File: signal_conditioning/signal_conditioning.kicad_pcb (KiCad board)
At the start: 2 copper layers, 16 parts, among them P1 CONN_6, P2 CONN_6, U1 LM324

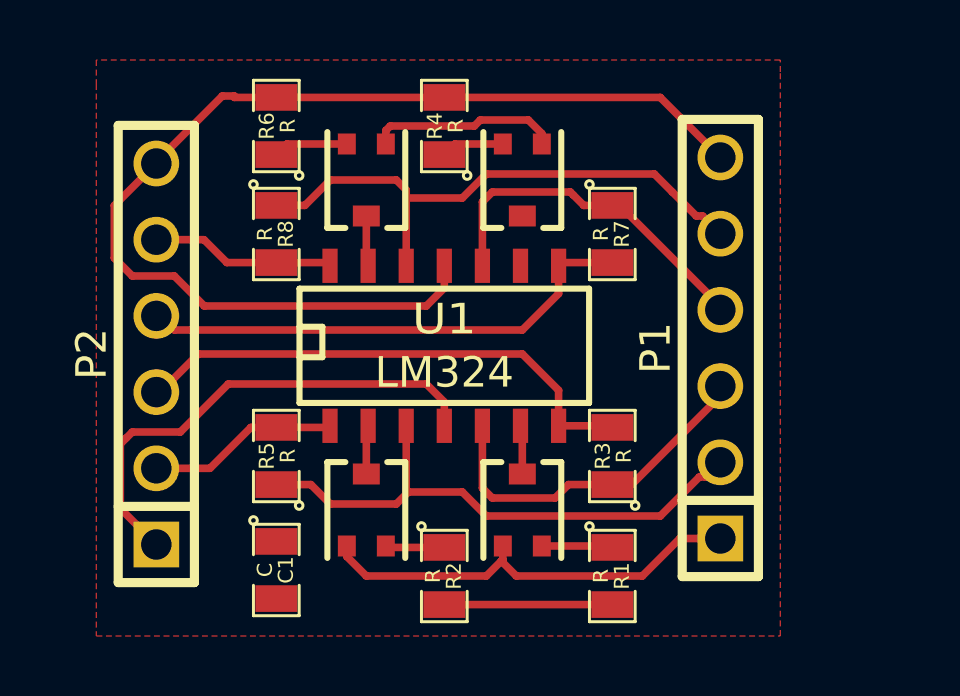
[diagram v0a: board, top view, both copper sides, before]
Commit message: rc version with pull ups input
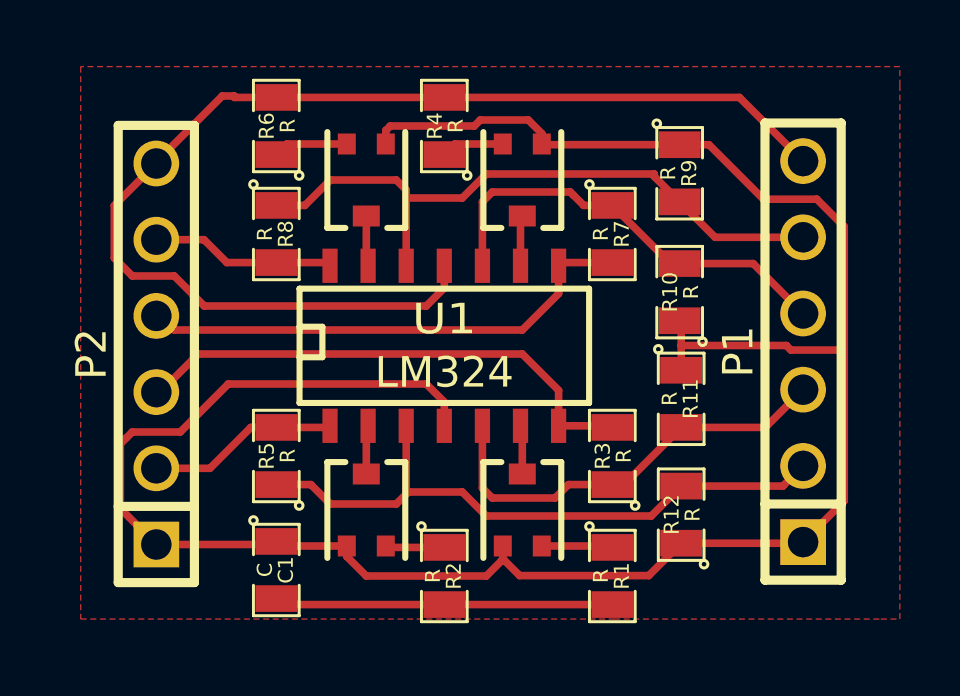
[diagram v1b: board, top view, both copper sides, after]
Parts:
- added R10: R, SM0805, F.Cu at (152.0, 91.3)
- added R11: R, SM0805, F.Cu at (152.1, 94.9)
- added R12: R, SM0805, F.Cu at (152.1, 98.8)
- added R9: R, SM0805, F.Cu at (152.0, 87.4)
- moved P1 2.76 mm to (156.2, 93.3)
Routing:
- net +3.3V: track 37.4 -> 75.9 mm
- net GND: track 42.6 -> 51.1 mm
- net /IN_4: track 19.0 -> 21.8 mm
- net /IN_2: track 11.9 -> 14.6 mm
- net /IN_1: track 18.6 -> 21.3 mm
- net /IN_3: track 11.9 -> 14.4 mm
- net N-0000018: track 0.00 -> 1.68 mm

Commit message: rc version with pull ups input
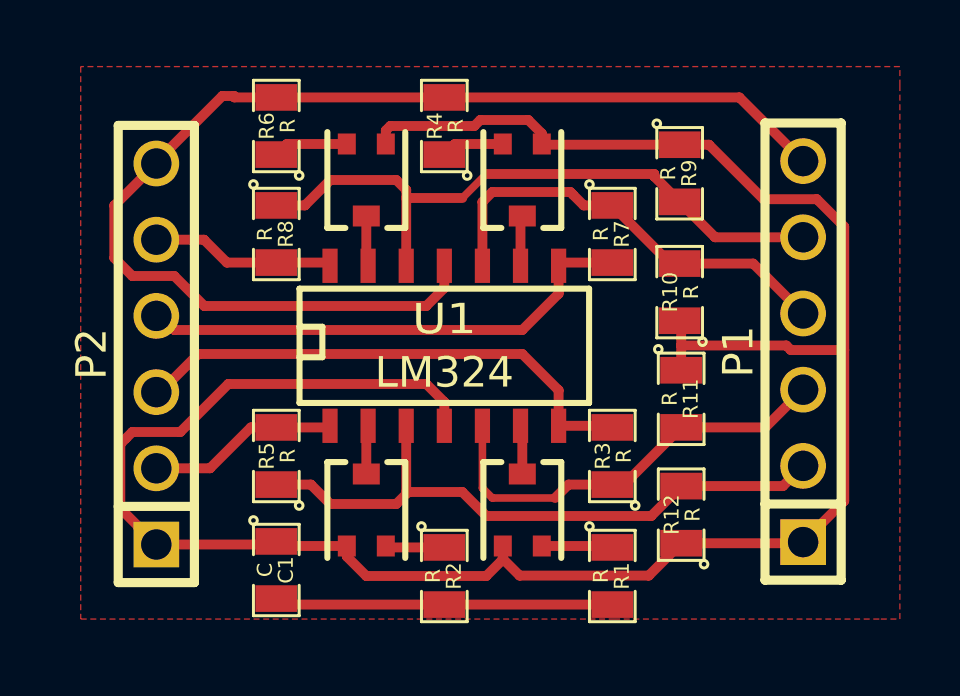
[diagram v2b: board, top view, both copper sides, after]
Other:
- net class Default: trace_width 0.254 -> 0.33
